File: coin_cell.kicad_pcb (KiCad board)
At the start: 2 copper layers, 34.9 x 29.8 mm, 11 parts, among them J1 Barrel_Jack, U1 NC7SZ14-D, U2 TPS61222

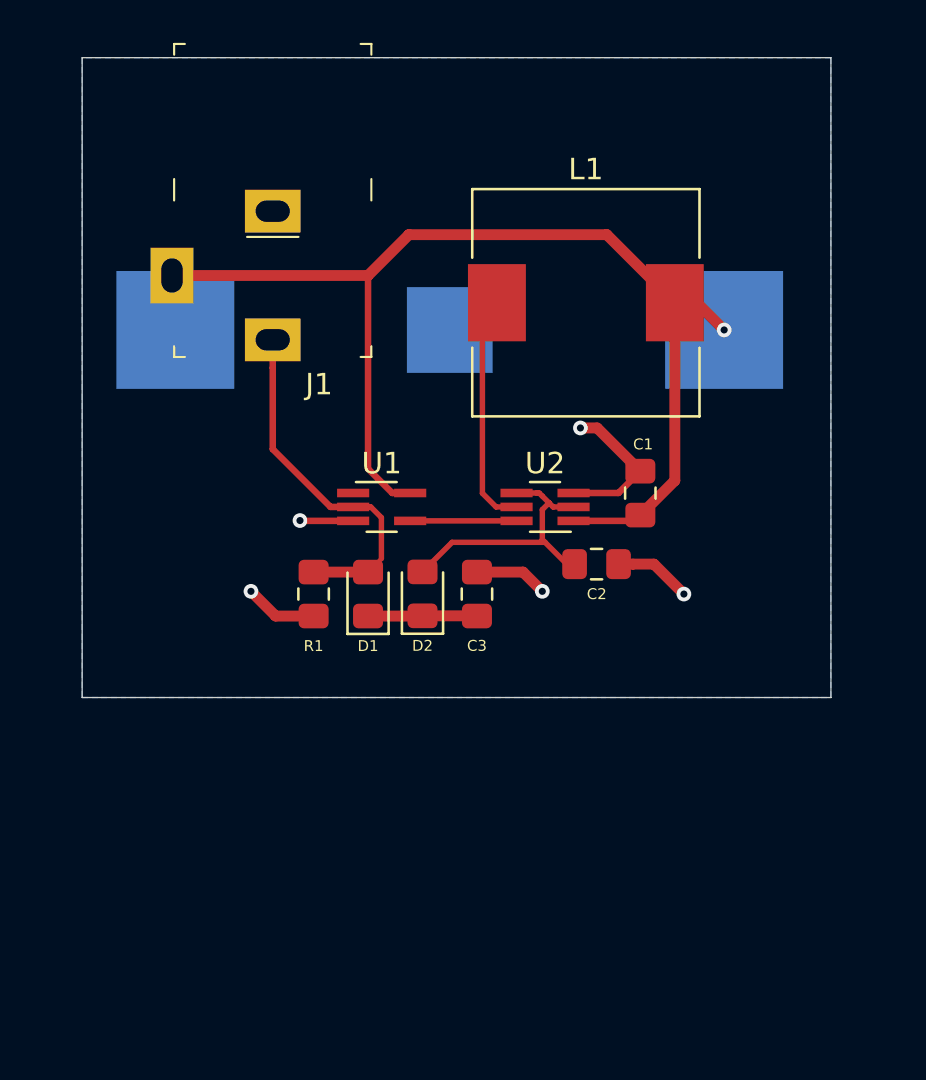
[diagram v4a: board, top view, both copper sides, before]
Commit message: Flipped S8211R 180 degrees and re-ran traces
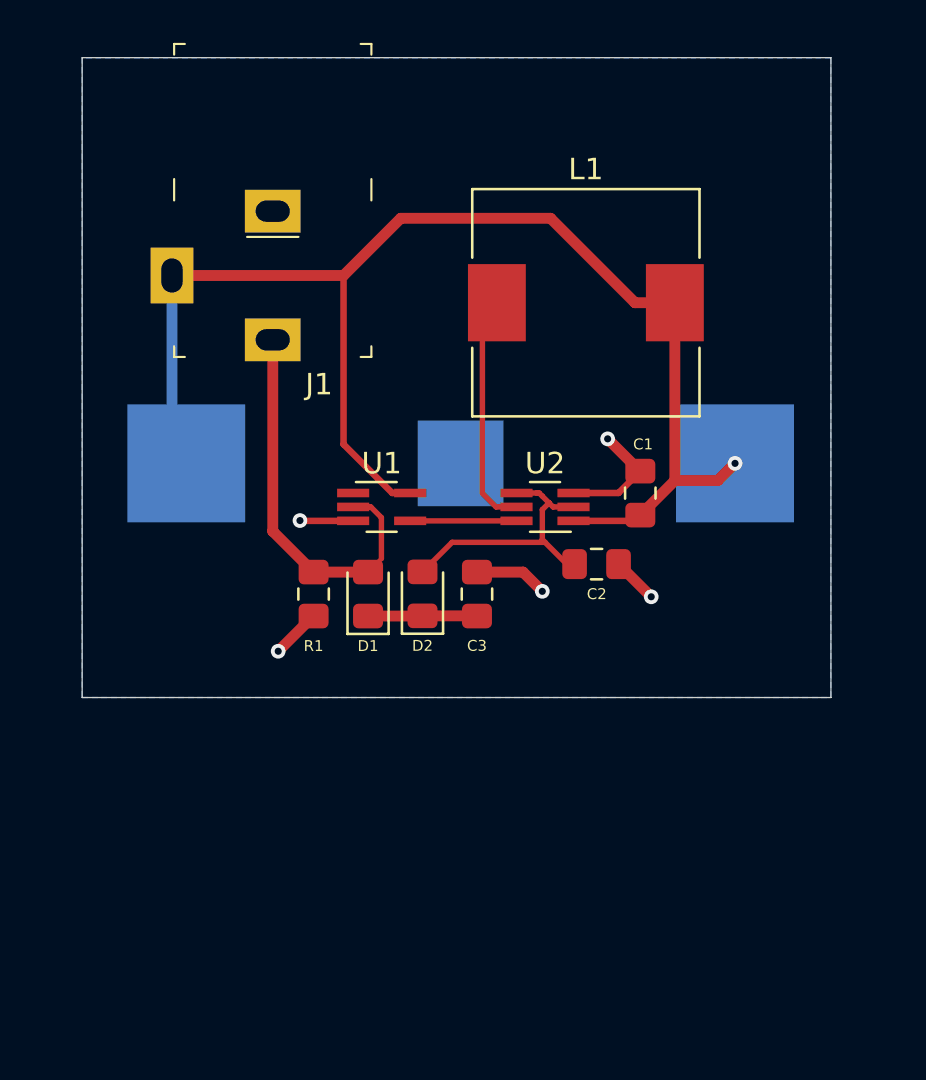
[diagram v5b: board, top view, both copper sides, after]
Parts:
- moved BT1 6.24 mm to (32.3, 32.9), turned to 0 degrees
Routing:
- net V_BATT: track 53.6 -> 64.1 mm
- net GND: track 20.1 -> 16.1 mm
- net 5V_WALL: track 16.8 -> 18.5 mm
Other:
- net class Default: trace_width 0.508 -> 0.3048
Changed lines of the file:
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@@
   )
   (setup
-    (last_trace_width 0.508)
+    (last_trace_width 0.3048)
     (trace_clearance 0.1524)
     (zone_clearance 0.508)
@@
   (net_class Default "This is the default net class."
     (clearance 0.1524)
-    (trace_width 0.508)
+    (trace_width 0.3048)
     (via_dia 0.6858)
     (via_drill 0.3302)
@@
   )
   (module coin_cell:S8211R (layer B.Cu)
-    (at 31.75 26.67 180)
+    (at 32.258 32.893)
     (fp_text reference BT1 (at 11.43 8.89) (layer B.SilkS)
       (effects (font (size 1 1) (thickness 0.15)) (justify mirror))
@@
     (fp_line (start -13 -7) (end -13 7) (layer B.SilkS) (width 0.12))
     (fp_line (start 13 -6) (end 0 -16) (layer B.SilkS) (width 0.12))
-    (pad 1 smd rect (at 12.8 0 180) (size 5.5 5.5) (layers B.Cu B.Paste B.Mask)
-      (net 1 V_BATT))
-    (pad 1 smd rect (at -12.8 0 180) (size 5.5 5.5) (layers B.Cu B.Paste B.Mask)
-      (net 1 V_BATT))
-    (pad 2 smd rect (at 0 0 180) (size 4 4) (layers B.Cu B.Paste B.Mask)
+    (pad 1 smd rect (at 12.8 0) (size 5.5 5.5) (layers B.Cu B.Paste B.Mask)
+      (net 1 V_BATT))
+    (pad 1 smd rect (at -12.8 0) (size 5.5 5.5) (layers B.Cu B.Paste B.Mask)
+      (net 1 V_BATT))
+    (pad 2 smd rect (at 0 0) (size 4 4) (layers B.Cu B.Paste B.Mask)
       (net 2 GND))
   )
@@
   (gr_line (start 14.605 43.815) (end 49.53 43.815) (layer Edge.Cuts) (width 0.05))
   (gr_line (start 14.605 13.97) (end 14.605 43.815) (layer Edge.Cuts) (width 0.05))
-  (via (at 44.55 26.67) (size 0.6858) (drill 0.3302) (layers F.Cu B.Cu) (net 1))
-  (segment (start 42.25 25.4) (end 43.28 25.4) (width 0.508) (layer F.Cu) (net 1))
-  (segment (start 43.28 25.4) (end 44.55 26.67) (width 0.508) (layer F.Cu) (net 1))
-  (segment (start 39.075 22.225) (end 42.25 25.4) (width 0.508) (layer F.Cu) (net 1))
-  (segment (start 29.845 22.225) (end 39.075 22.225) (width 0.508) (layer F.Cu) (net 1))
-  (segment (start 27.94 24.13) (end 29.845 22.225) (width 0.508) (layer F.Cu) (net 1))
-  (segment (start 27.94 24.13) (end 18.795 24.13) (width 0.508) (layer F.Cu) (net 1))
   (segment (start 40.371 35.575) (end 40.64 35.306) (width 0.3048) (layer F.Cu) (net 1))
   (segment (start 37.525 35.575) (end 40.371 35.575) (width 0.3048) (layer F.Cu) (net 1))
   (segment (start 42.25 33.696) (end 42.25 25.4) (width 0.508) (layer F.Cu) (net 1))
   (segment (start 40.64 35.306) (end 42.25 33.696) (width 0.508) (layer F.Cu) (net 1))
-  (segment (start 27.94 33.147) (end 27.94 24.13) (width 0.3048) (layer F.Cu) (net 1))
+  (segment (start 18.796 24.131) (end 18.795 24.13) (width 0.508) (layer B.Cu) (net 1))
+  (segment (start 19.458 32.893) (end 18.796 32.231) (width 0.508) (layer B.Cu) (net 1))
+  (segment (start 18.796 32.231) (end 18.796 24.131) (width 0.508) (layer B.Cu) (net 1))
+  (via (at 45.058 32.893) (size 0.6858) (drill 0.3302) (layers F.Cu B.Cu) (net 1))
+  (segment (start 42.25 33.696) (end 44.255 33.696) (width 0.508) (layer F.Cu) (net 1))
+  (segment (start 44.255 33.696) (end 45.058 32.893) (width 0.508) (layer F.Cu) (net 1))
+  (segment (start 18.795 24.13) (end 26.797 24.13) (width 0.508) (layer F.Cu) (net 1))
+  (segment (start 26.797 24.13) (end 29.464 21.463) (width 0.508) (layer F.Cu) (net 1))
+  (segment (start 40.392 25.4) (end 42.25 25.4) (width 0.508) (layer F.Cu) (net 1))
+  (segment (start 36.455 21.463) (end 40.392 25.4) (width 0.508) (layer F.Cu) (net 1))
+  (segment (start 29.464 21.463) (end 36.455 21.463) (width 0.508) (layer F.Cu) (net 1))
+  (segment (start 26.797 32.004) (end 26.797 24.13) (width 0.3048) (layer F.Cu) (net 1))
   (segment (start 29.905 34.275) (end 29.068 34.275) (width 0.3048) (layer F.Cu) (net 1))
-  (segment (start 29.068 34.275) (end 27.94 33.147) (width 0.3048) (layer F.Cu) (net 1))
+  (segment (start 29.068 34.275) (end 26.797 32.004) (width 0.3048) (layer F.Cu) (net 1))
   (via (at 24.765 35.56) (size 0.6858) (drill 0.3302) (layers F.Cu B.Cu) (net 2))
   (segment (start 27.245 35.575) (end 24.78 35.575) (width 0.3048) (layer F.Cu) (net 2))
@@
   (segment (start 39.621 34.275) (end 40.64 33.256) (width 0.3048) (layer F.Cu) (net 2))
   (segment (start 37.525 34.275) (end 39.621 34.275) (width 0.3048) (layer F.Cu) (net 2))
-  (via (at 37.846 31.242) (size 0.6858) (drill 0.3302) (layers F.Cu B.Cu) (net 2))
-  (segment (start 40.64 33.256) (end 38.626 31.242) (width 0.508) (layer F.Cu) (net 2))
-  (segment (start 38.626 31.242) (end 37.846 31.242) (width 0.508) (layer F.Cu) (net 2))
-  (via (at 22.479 38.862) (size 0.6858) (drill 0.3302) (layers F.Cu B.Cu) (net 2))
-  (segment (start 25.4 40.014) (end 23.631 40.014) (width 0.508) (layer F.Cu) (net 2))
-  (segment (start 23.631 40.014) (end 22.479 38.862) (width 0.508) (layer F.Cu) (net 2))
-  (segment (start 39.624 37.592) (end 40.299 37.592) (width 0.508) (layer F.Cu) (net 2))
-  (via (at 42.672 38.989) (size 0.6858) (drill 0.3302) (layers F.Cu B.Cu) (net 2))
-  (segment (start 40.299 37.592) (end 41.275 37.592) (width 0.508) (layer F.Cu) (net 2))
-  (segment (start 41.275 37.592) (end 42.672 38.989) (width 0.508) (layer F.Cu) (net 2))
   (via (at 36.068 38.862) (size 0.6858) (drill 0.3302) (layers F.Cu B.Cu) (net 2))
   (segment (start 33.02 37.964) (end 35.17 37.964) (width 0.508) (layer F.Cu) (net 2))
   (segment (start 35.17 37.964) (end 36.068 38.862) (width 0.508) (layer F.Cu) (net 2))
+  (via (at 41.148 39.116) (size 0.6858) (drill 0.3302) (layers F.Cu B.Cu) (net 2))
+  (segment (start 39.624 37.592) (end 41.148 39.116) (width 0.508) (layer F.Cu) (net 2))
+  (via (at 23.749 41.656) (size 0.6858) (drill 0.3302) (layers F.Cu B.Cu) (net 2))
+  (segment (start 25.4 40.014) (end 25.391 40.014) (width 0.508) (layer F.Cu) (net 2))
+  (segment (start 25.391 40.014) (end 23.749 41.656) (width 0.508) (layer F.Cu) (net 2))
+  (via (at 39.116 31.75) (size 0.6858) (drill 0.3302) (layers F.Cu B.Cu) (net 2))
+  (segment (start 40.64 33.256) (end 40.622 33.256) (width 0.508) (layer F.Cu) (net 2))
+  (segment (start 40.622 33.256) (end 39.116 31.75) (width 0.508) (layer F.Cu) (net 2))
   (segment (start 35.8182 34.275) (end 34.865 34.275) (width 0.254) (layer F.Cu) (net 3))
   (segment (start 35.9218 34.275) (end 35.8182 34.275) (width 0.254) (layer F.Cu) (net 3))
@@
   (segment (start 33.011 40.005) (end 33.02 40.014) (width 0.508) (layer F.Cu) (net 4))
   (segment (start 30.48 40.005) (end 33.011 40.005) (width 0.508) (layer F.Cu) (net 4))
-  (segment (start 23.495 28.4348) (end 23.495 27.13) (width 0.3048) (layer F.Cu) (net 5))
-  (segment (start 23.495 32.2298) (end 23.495 28.4348) (width 0.3048) (layer F.Cu) (net 5))
-  (segment (start 26.1902 34.925) (end 23.495 32.2298) (width 0.3048) (layer F.Cu) (net 5))
-  (segment (start 27.245 34.925) (end 26.1902 34.925) (width 0.3048) (layer F.Cu) (net 5))
   (segment (start 28.067 34.925) (end 27.245 34.925) (width 0.254) (layer F.Cu) (net 5))
   (segment (start 28.563372 35.421372) (end 28.067 34.925) (width 0.254) (layer F.Cu) (net 5))
@@
   (segment (start 28.563372 37.340628) (end 28.563372 35.421372) (width 0.254) (layer F.Cu) (net 5))
   (segment (start 25.4 37.964) (end 27.94 37.964) (width 0.508) (layer F.Cu) (net 5))
+  (segment (start 23.495 36.059) (end 25.4 37.964) (width 0.508) (layer F.Cu) (net 5))
+  (segment (start 23.495 27.13) (end 23.495 36.059) (width 0.508) (layer F.Cu) (net 5))
   (segment (start 33.95 25.85) (end 33.95 25.4) (width 0.2032) (layer F.Cu) (net 6))
   (segment (start 33.274 26.526) (end 33.95 25.85) (width 0.254) (layer F.Cu) (net 6))

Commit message: Increase edge cut thickness to 4 mil
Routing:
- net GND: track 16.1 -> 14.8 mm
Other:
- net class Default: trace_width 0.3048 -> 0.508
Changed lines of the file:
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@@
     (thickness 1.6)
     (drawings 4)
-    (tracks 64)
+    (tracks 63)
     (zones 0)
     (modules 11)
@@
   )
   (setup
-    (last_trace_width 0.3048)
+    (last_trace_width 0.508)
     (trace_clearance 0.1524)
     (zone_clearance 0.508)
@@
   (net_class Default "This is the default net class."
     (clearance 0.1524)
-    (trace_width 0.3048)
+    (trace_width 0.508)
     (via_dia 0.6858)
     (via_drill 0.3302)
@@
   (module coin_cell:Barrel_Jack_Small_Hole_Type_5.5mmODx2.1mmID_PJ-102A (layer F.Cu)
     (at 23.495 24.13)
-    (fp_text reference J1 (at 2.159 5.08) (layer F.SilkS)
+    (fp_text reference J1 (at -2.54 5.207) (layer F.SilkS)
       (effects (font (size 1 1) (thickness 0.15)))
     )
@@
     )
   )
-  (gr_line (start 49.53 13.97) (end 14.605 13.97) (layer Edge.Cuts) (width 0.05))
-  (gr_line (start 49.53 43.815) (end 49.53 13.97) (layer Edge.Cuts) (width 0.05))
-  (gr_line (start 14.605 43.815) (end 49.53 43.815) (layer Edge.Cuts) (width 0.05))
-  (gr_line (start 14.605 13.97) (end 14.605 43.815) (layer Edge.Cuts) (width 0.05))
+  (gr_line (start 49.53 13.97) (end 14.605 13.97) (layer Edge.Cuts) (width 0.1016))
+  (gr_line (start 49.53 43.815) (end 49.53 13.97) (layer Edge.Cuts) (width 0.1016))
+  (gr_line (start 14.605 43.815) (end 49.53 43.815) (layer Edge.Cuts) (width 0.1016))
+  (gr_line (start 14.605 13.97) (end 14.605 43.815) (layer Edge.Cuts) (width 0.1016))
   (segment (start 40.371 35.575) (end 40.64 35.306) (width 0.3048) (layer F.Cu) (net 1))
   (segment (start 37.525 35.575) (end 40.371 35.575) (width 0.3048) (layer F.Cu) (net 1))
-  (segment (start 42.25 33.696) (end 42.25 25.4) (width 0.508) (layer F.Cu) (net 1))
   (segment (start 40.64 35.306) (end 42.25 33.696) (width 0.508) (layer F.Cu) (net 1))
   (segment (start 18.796 24.131) (end 18.795 24.13) (width 0.508) (layer B.Cu) (net 1))
@@
   (segment (start 18.796 32.231) (end 18.796 24.131) (width 0.508) (layer B.Cu) (net 1))
   (via (at 45.058 32.893) (size 0.6858) (drill 0.3302) (layers F.Cu B.Cu) (net 1))
-  (segment (start 42.25 33.696) (end 44.255 33.696) (width 0.508) (layer F.Cu) (net 1))
-  (segment (start 44.255 33.696) (end 45.058 32.893) (width 0.508) (layer F.Cu) (net 1))
   (segment (start 18.795 24.13) (end 26.797 24.13) (width 0.508) (layer F.Cu) (net 1))
-  (segment (start 26.797 24.13) (end 29.464 21.463) (width 0.508) (layer F.Cu) (net 1))
-  (segment (start 40.392 25.4) (end 42.25 25.4) (width 0.508) (layer F.Cu) (net 1))
-  (segment (start 36.455 21.463) (end 40.392 25.4) (width 0.508) (layer F.Cu) (net 1))
-  (segment (start 29.464 21.463) (end 36.455 21.463) (width 0.508) (layer F.Cu) (net 1))
   (segment (start 26.797 32.004) (end 26.797 24.13) (width 0.3048) (layer F.Cu) (net 1))
   (segment (start 29.905 34.275) (end 29.068 34.275) (width 0.3048) (layer F.Cu) (net 1))
   (segment (start 29.068 34.275) (end 26.797 32.004) (width 0.3048) (layer F.Cu) (net 1))
+  (segment (start 42.25 33.696) (end 42.25 25.4) (width 0.508) (layer F.Cu) (net 1))
+  (segment (start 42.25 33.696) (end 44.255 33.696) (width 0.508) (layer F.Cu) (net 1))
+  (segment (start 44.255 33.696) (end 45.058 32.893) (width 0.508) (layer F.Cu) (net 1))
+  (segment (start 29.464 21.463) (end 38.313 21.463) (width 0.508) (layer F.Cu) (net 1))
+  (segment (start 26.797 24.13) (end 29.464 21.463) (width 0.508) (layer F.Cu) (net 1))
+  (segment (start 38.313 21.463) (end 42.25 25.4) (width 0.508) (layer F.Cu) (net 1))
   (via (at 24.765 35.56) (size 0.6858) (drill 0.3302) (layers F.Cu B.Cu) (net 2))
   (segment (start 27.245 35.575) (end 24.78 35.575) (width 0.3048) (layer F.Cu) (net 2))
@@
   (segment (start 39.621 34.275) (end 40.64 33.256) (width 0.3048) (layer F.Cu) (net 2))
   (segment (start 37.525 34.275) (end 39.621 34.275) (width 0.3048) (layer F.Cu) (net 2))
-  (via (at 36.068 38.862) (size 0.6858) (drill 0.3302) (layers F.Cu B.Cu) (net 2))
-  (segment (start 33.02 37.964) (end 35.17 37.964) (width 0.508) (layer F.Cu) (net 2))
-  (segment (start 35.17 37.964) (end 36.068 38.862) (width 0.508) (layer F.Cu) (net 2))
   (via (at 41.148 39.116) (size 0.6858) (drill 0.3302) (layers F.Cu B.Cu) (net 2))
   (segment (start 39.624 37.592) (end 41.148 39.116) (width 0.508) (layer F.Cu) (net 2))
@@
   (segment (start 40.64 33.256) (end 40.622 33.256) (width 0.508) (layer F.Cu) (net 2))
   (segment (start 40.622 33.256) (end 39.116 31.75) (width 0.508) (layer F.Cu) (net 2))
+  (via (at 35.179 37.973) (size 0.6858) (drill 0.3302) (layers F.Cu B.Cu) (net 2))
+  (segment (start 33.02 37.964) (end 35.17 37.964) (width 0.508) (layer F.Cu) (net 2))
+  (segment (start 35.17 37.964) (end 35.179 37.973) (width 0.508) (layer F.Cu) (net 2))
   (segment (start 35.8182 34.275) (end 34.865 34.275) (width 0.254) (layer F.Cu) (net 3))
   (segment (start 35.9218 34.275) (end 35.8182 34.275) (width 0.254) (layer F.Cu) (net 3))
